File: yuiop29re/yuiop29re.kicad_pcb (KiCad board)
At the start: 2 copper layers, 116.5 x 116.5 mm, 123 parts, among them J1 USB_C_Receptacle_USB2.0_16P, J2 SSD1306 OLED, J3 AudioJack4, J4 UART0, J5 SWD, Q1 BSS138, U1 RP2040_breakout

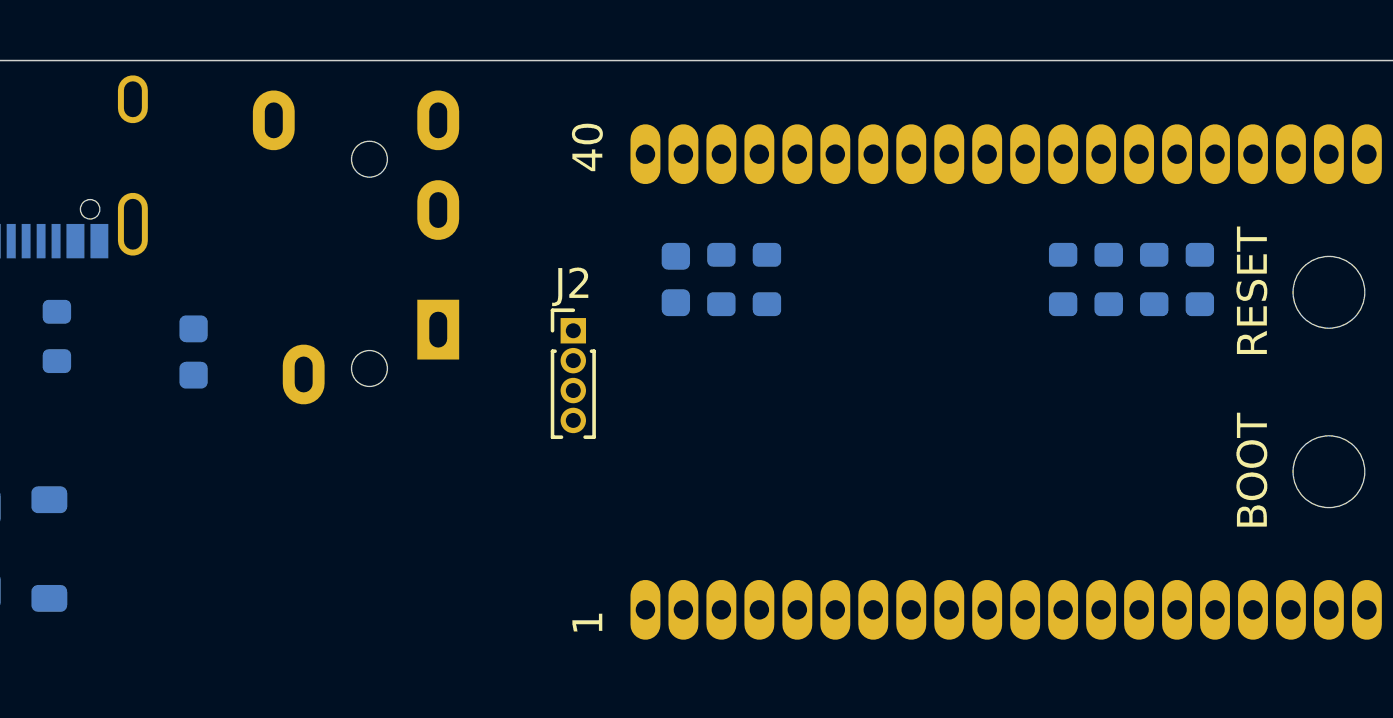
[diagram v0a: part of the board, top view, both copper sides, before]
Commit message: yuiop29re: improve TRRS jack
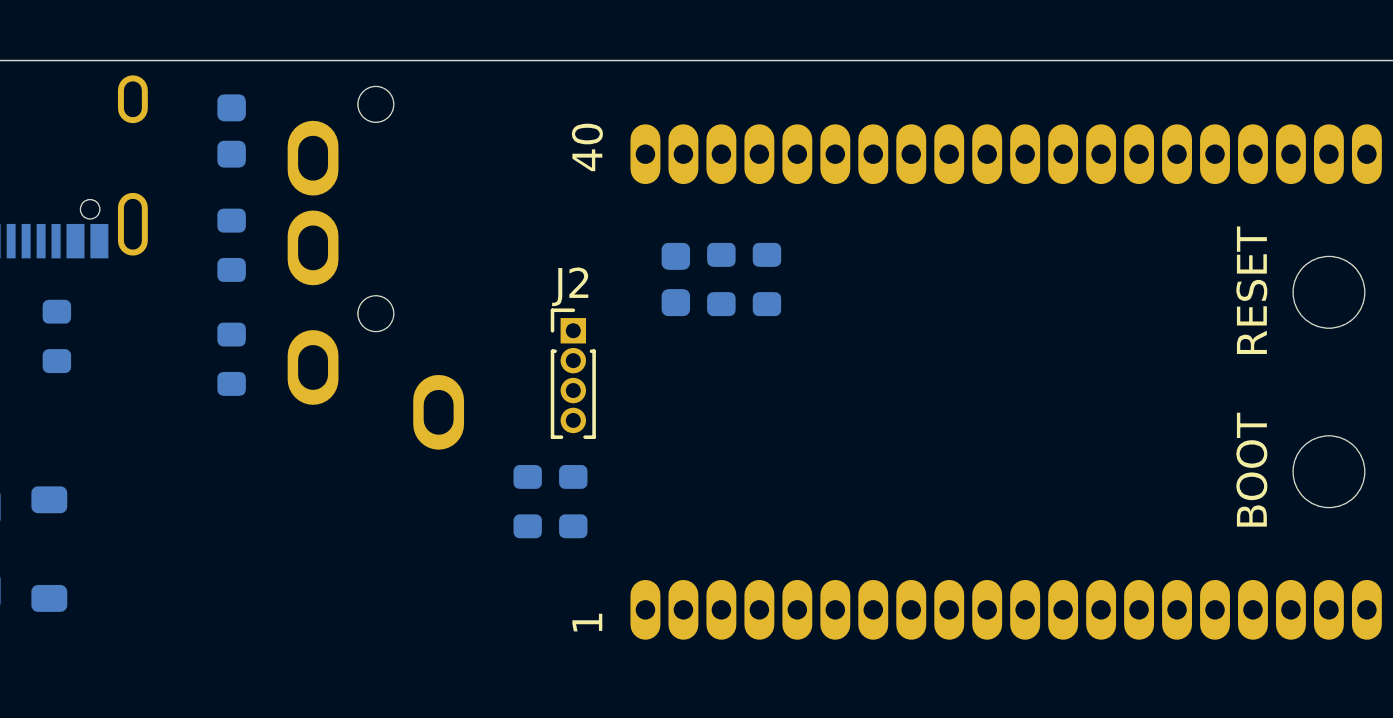
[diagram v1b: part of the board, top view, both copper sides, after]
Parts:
- J3: value AudioJack4 -> MJ-4PP-9; footprint Connector_Audio:Jack_3.5mm_PJ320E_Horizontal -> yuiop:MJ-4PP-9
- moved R10 32.5 mm to (157.6, 51.7)
- moved R9 30.9 mm to (157.6, 47.9)
- moved R7 19.4 mm to (167.5, 56.5)
- moved R8 19.4 mm to (169.1, 56.5)
- moved C6 7.50 mm to (157.6, 44.1)
- moved J3 3.60 mm to (162.4, 47.8)

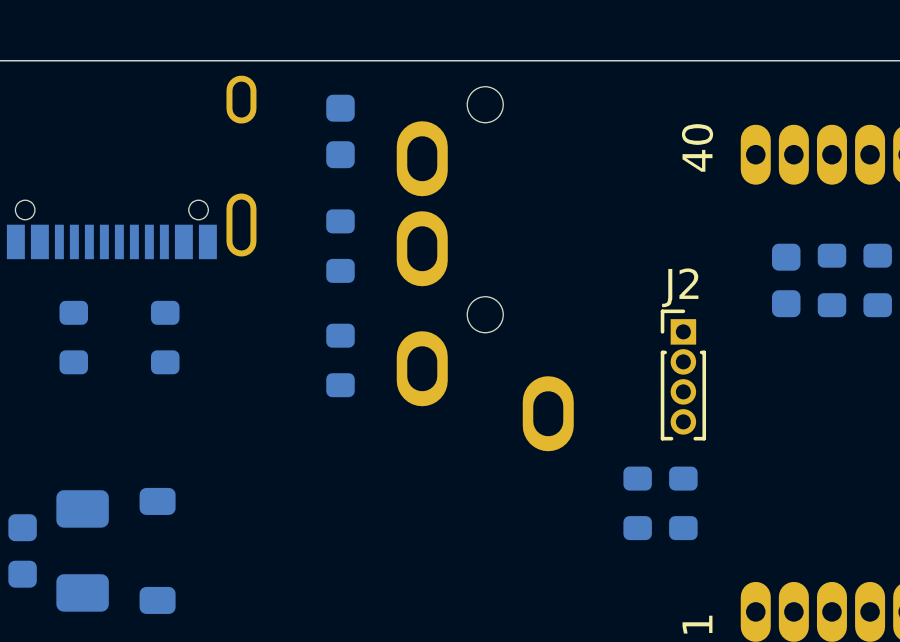
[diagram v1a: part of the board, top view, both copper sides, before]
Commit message: update TRRS jack footprint to new version
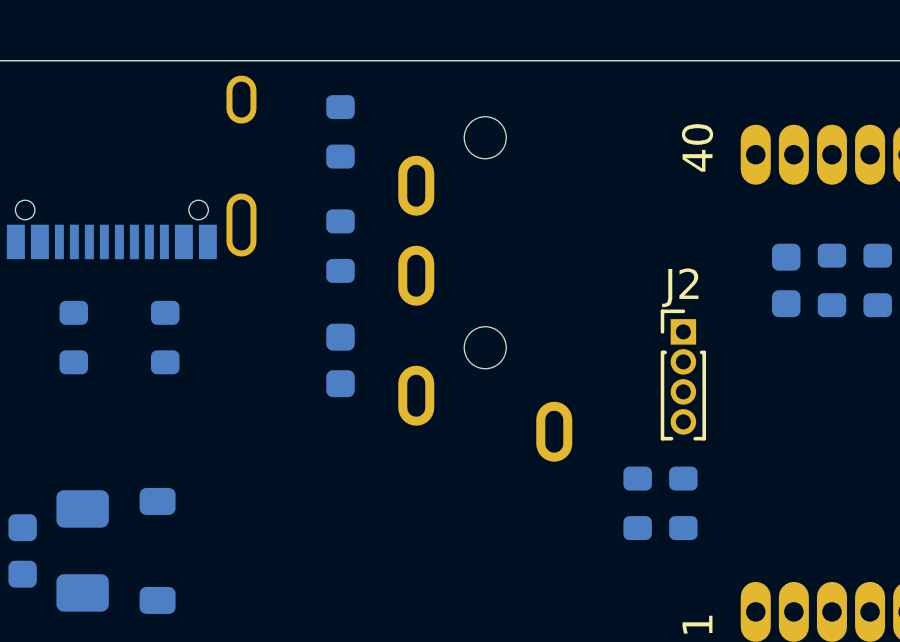
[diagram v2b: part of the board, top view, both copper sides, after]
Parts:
- J3: footprint yuiop:MJ-4PP-9 -> yuiop:MJ-4PP-9_2021
- moved C6 7.63 mm to (157.6, 51.7)
- moved R10 3.81 mm to (157.6, 47.9), turned to 90 degrees
- moved R9 3.81 mm to (157.6, 44.1), turned to 90 degrees

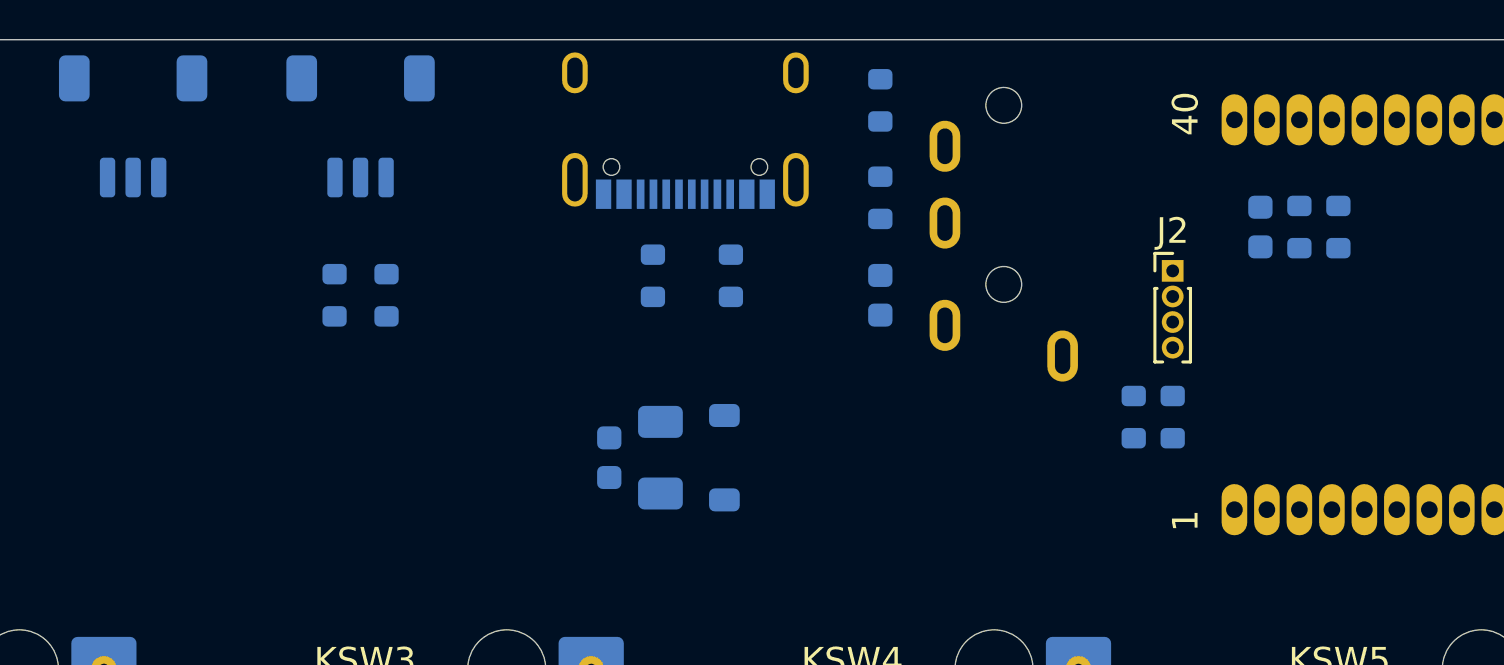
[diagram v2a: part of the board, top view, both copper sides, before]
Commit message: fix OLED footprint
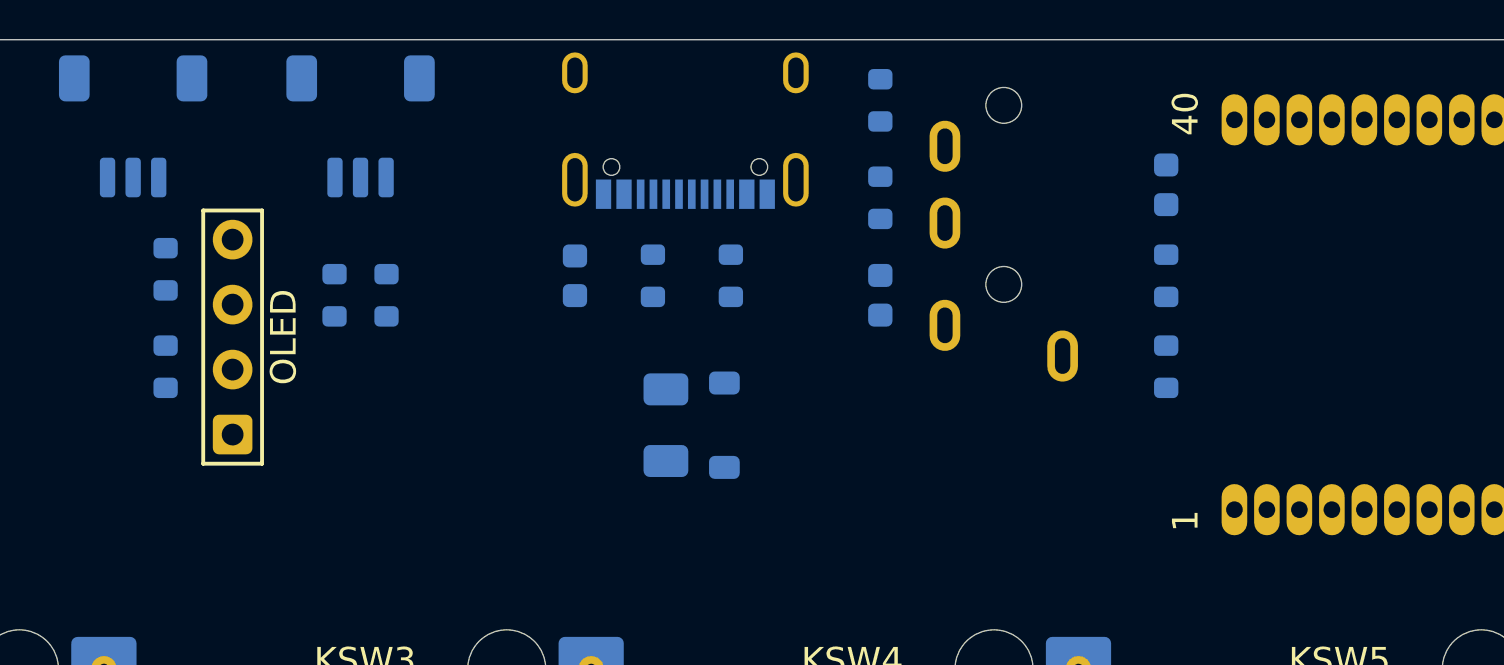
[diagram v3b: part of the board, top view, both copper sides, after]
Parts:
- J2: footprint Connector_PinHeader_1.00mm:PinHeader_1x04_P1.00mm_Vertical -> yuiop:OLED_128x32
- moved R8 39.8 mm to (129.7, 50.7)
- moved R7 37.9 mm to (129.7, 54.5)
- moved J2 19.1 mm to (150.0, 52.4), turned to 90 degrees
- moved R4 8.67 mm to (168.8, 54.5)
- moved C1 7.24 mm to (145.7, 51.0)
- moved R3 5.54 mm to (168.8, 51.0)
- moved C2 4.04 mm to (168.8, 47.4), turned to 90 degrees
- moved F1 1.29 mm to (149.2, 56.8)
- moved DS1 1.27 mm to (151.5, 56.8)

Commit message: yuiop29re: wiring completed
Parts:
- moved C5 16.4 mm to (197.8, 152.6), turned to 90 degrees
- moved C3 3.69 mm to (98.2, 81.2)
- moved C6 2.97 mm to (160.4, 50.7)
- moved R9 2.84 mm to (160.4, 44.6)
- moved R10 2.81 mm to (160.4, 47.7)
- moved J3 2.79 mm to (165.2, 47.8)
- moved R4 2.65 mm to (171.3, 53.8)
- moved C2 2.55 mm to (171.3, 47.7)
- moved R3 2.55 mm to (171.3, 50.7)
- moved U1 2.03 mm to (185.6, 52.5)
- moved F1 1.78 mm to (147.5, 56.8)
- moved DS1 1.02 mm to (152.5, 56.8)
- turned C4 to -90 degrees
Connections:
- R3 pad 2: /USB_DM -> /USB_DP
- R4 pad 2: /USB_DP -> /USB_DM
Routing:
- net GND: track 0.00 -> 881.4 mm, vias 0 -> 38
- net /5V0: track 0.00 -> 780.4 mm, vias 0 -> 2
- net /ROW5: track 78.7 -> 267.4 mm, vias 0 -> 2
- net /3V3: track 0.00 -> 133.1 mm, vias 0 -> 3
- net /COL1: track 57.1 -> 159.0 mm, vias 0 -> 1
- net /SWDIO: track 0.00 -> 89.2 mm
- net /SWDCLK: track 0.00 -> 86.3 mm
- net /ROW4: track 98.4 -> 184.4 mm, vias 0 -> 1
- net /RE1_B: track 0.00 -> 74.2 mm
- net /LED_D_3V3: track 0.00 -> 71.5 mm
- net /COL2: track 80.1 -> 150.8 mm
- net /UART0_RX: track 0.00 -> 69.9 mm, vias 0 -> 1
- net /I2C0_SDA: track 0.00 -> 69.3 mm, vias 0 -> 1
- net /I2C0_SCLK: track 0.00 -> 68.9 mm, vias 0 -> 1
- net /UART0_TX: track 0.00 -> 67.3 mm
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- added copper zone on B.Cu, net GND
- added copper zone on F.Cu, net GND

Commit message: yuiop29re: add JLC serial position mark
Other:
- board text added: "JLCJLCJLCJLC"
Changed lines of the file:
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@@
 		(layer "Edge.Cuts")
+	)
+	(gr_text "JLCJLCJLCJLC"
+		(at 101.8 148 0)
+		(layer "B.SilkS")
+		(effects
+			(font
+				(size 0.8 0.8)
+				(thickness 0.15)
+			)
+			(justify left bottom mirror)
+		)
 	)
 	(segment

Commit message: yiuop29re: add product marks
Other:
- board text added: "YUIOP29RE"
- board text added: "designed by KoRoN/KaoriYa"
- board text added: "revision 1"
